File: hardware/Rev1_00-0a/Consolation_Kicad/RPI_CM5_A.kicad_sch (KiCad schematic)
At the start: 63 parts, among them J17 61300311121, J19 RPI_CMx_A, J7 2998TR, Q19 SSM3K56FS,LF, Q20 SSM3K56FS,LF, Q21 SSM3K56FS,LF, Q22 SSM3K56FS,LF, Q26 SSM3K56FS,LF, Q27 SSM3K56FS,LF, Q28 SSM3K56FS,LF, Q29 SSM3K56FS,LF, U19 SN74LVC1G125DBVR, U21 MCP7940NT-I/MS, Y2 32.768kHz

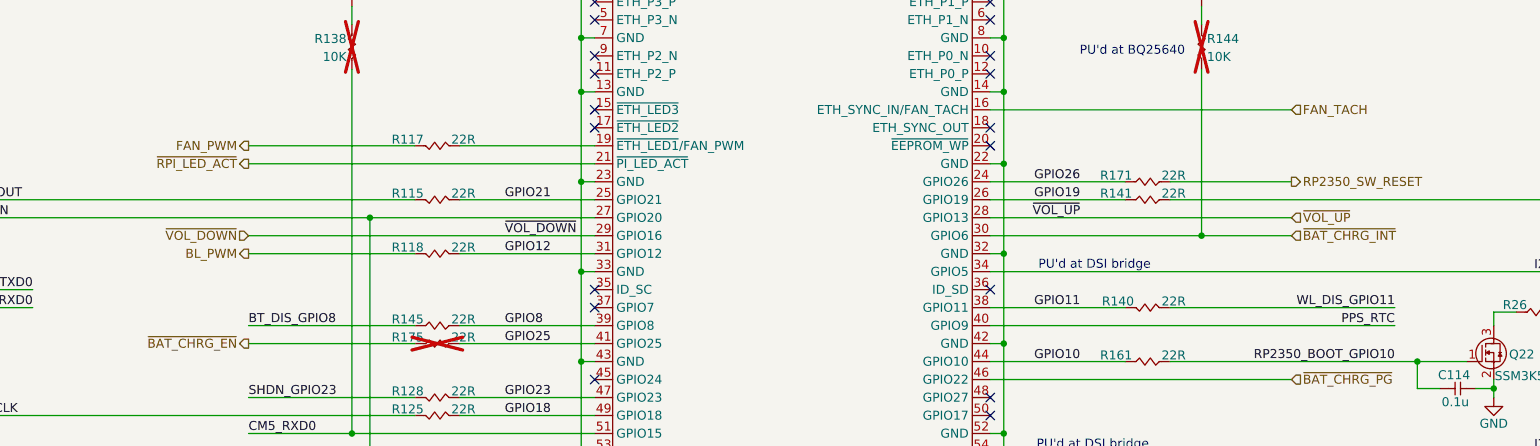
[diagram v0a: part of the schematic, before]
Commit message: Routing Adjust PinMux to ease routing
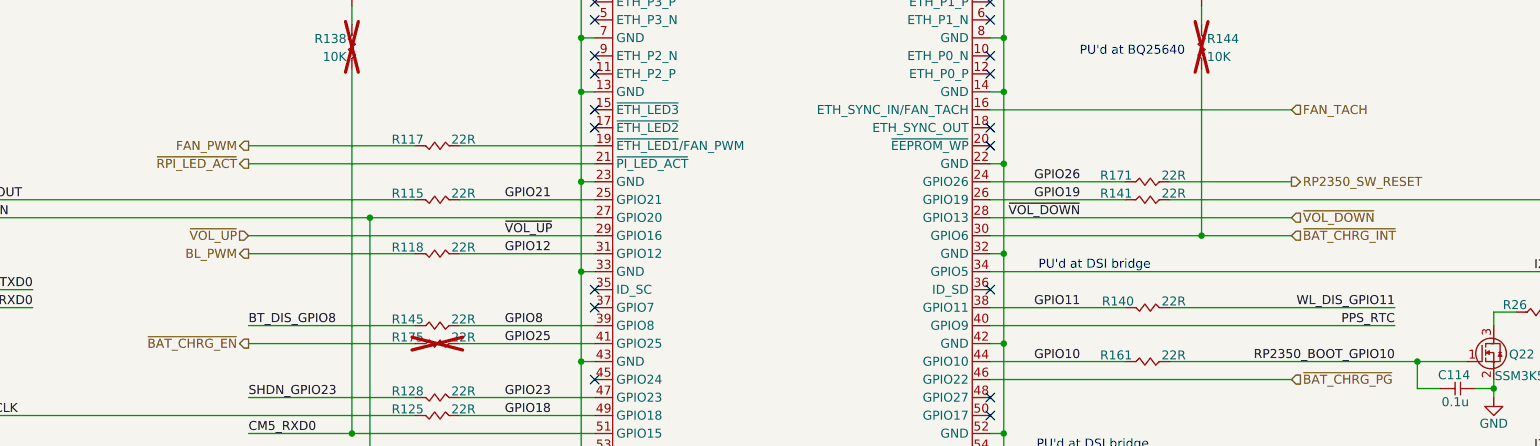
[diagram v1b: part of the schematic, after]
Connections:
- net ~{VOL_DOWN}: now also J19.28 (GPIO13); no longer J19.29 (GPIO16)
- net ~{VOL_UP}: now also J19.29 (GPIO16); no longer J19.28 (GPIO13)
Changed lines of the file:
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@@
 	(title_block
 		(title "Consolation [Console Emulation]")
-		(date "2026-10-12")
+		(date "2026-10-25")
 		(rev "1.00-0A")
 		(comment 1 "Jean-Francois Bilodeau")
@@
 	)
 	(bus_entry
+		(at 31.115 75.565)
+		(size 2.54 2.54)
+		(stroke
+			(width 0)
+			(type default)
+		)
+	)
+	(bus_entry
 		(at 31.115 85.725)
 		(size 2.54 2.54)
@@
 	)
 	(bus_entry
-		(at 31.115 75.565)
-		(size 2.54 2.54)
-		(stroke
-			(width 0)
-			(type default)
-		)
-	)
-	(bus_entry
 		(at 31.115 90.805)
 		(size 2.54 2.54)
@@
 		)
 	)
-	(bus
-		(pts
-			(xy 28.575 73.025) (xy 31.115 75.565)
-		)
-		(stroke
-			(width 0)
-			(type default)
-		)
-	)
 	(wire
 		(pts
@@
 	(wire
 		(pts
-			(xy 33.655 78.105) (xy 97.79 78.105)
+			(xy 106.045 172.085) (xy 107.315 172.085)
 		)
 		(stroke
@@
 	(wire
 		(pts
-			(xy 106.045 172.085) (xy 107.315 172.085)
+			(xy 137.795 178.435) (xy 137.795 184.15)
 		)
 		(stroke
@@
 	(wire
 		(pts
-			(xy 137.795 178.435) (xy 137.795 184.15)
+			(xy 29.21 139.065) (xy 29.21 142.875)
 		)
 		(stroke
@@
 	(wire
 		(pts
-			(xy 29.21 139.065) (xy 29.21 142.875)
+			(xy 33.655 50.165) (xy 91.44 50.165)
 		)
 		(stroke
@@
 	(wire
 		(pts
-			(xy 33.655 50.165) (xy 91.44 50.165)
+			(xy 102.235 118.745) (xy 102.235 120.015)
 		)
 		(stroke
@@
 	(wire
 		(pts
-			(xy 102.235 118.745) (xy 102.235 120.015)
+			(xy 239.395 159.385) (xy 239.395 160.655)
 		)
 		(stroke
@@
 	(wire
 		(pts
-			(xy 239.395 159.385) (xy 239.395 160.655)
+			(xy 179.07 83.185) (xy 268.605 83.185)
 		)
 		(stroke
@@
 	(wire
 		(pts
-			(xy 179.07 83.185) (xy 268.605 83.185)
+			(xy 33.655 78.105) (xy 97.79 78.105)
 		)
 		(stroke
@@
 		)
 	)
+	(bus
+		(pts
+			(xy 28.575 73.025) (xy 31.115 75.565)
+		)
+		(stroke
+			(width 0)
+			(type default)
+		)
+	)
 	(wire
 		(pts
@@
 		)
 	)
-	(label "~{VOL_DOWN}"
+	(label "~{VOL_UP}"
 		(at 110.49 52.705 0)
 		(effects
@@
 		)
 	)
-	(label "~{VOL_UP}"
+	(label "~{VOL_DOWN}"
 		(at 191.77 50.165 180)
 		(effects
@@
 		)
 	)
-	(hierarchical_label "~{VOL_DOWN}"
+	(hierarchical_label "~{VOL_UP}"
 		(shape input)
 		(at 74.295 52.705 180)
@@
 		)
 	)
-	(hierarchical_label "~{VOL_UP}"
+	(hierarchical_label "~{VOL_DOWN}"
 		(shape input)
 		(at 221.615 50.165 0)

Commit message: Add preliminary manufacturing files for Consolation Review pinout & design notes
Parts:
- added R165: 10K, footprint:RES_0402, symbol KicadCompDb:Resistors/RES_SMT_00013
- R144: now fitted
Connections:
- net 3V3: now also R165.2
- net ~{BAT_CHRG_PG}: now also R165.1
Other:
- note removed: "PU'd at BQ25640"

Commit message: Work on DFM, Pick N Place file accuracy, BOM accuracy Generating output files regularly through incremental updates
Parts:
- J19: value RPI_CMx_A -> DF40HC(3.0)-100DS-0.4V
- TP54, TP55: now left out of the parts list
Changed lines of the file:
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@@
 		(body_style 1)
 		(exclude_from_sim no)
-		(in_bom yes)
+		(in_bom no)
 		(on_board yes)
-		(in_pos_files yes)
+		(in_pos_files no)
 		(dnp no)
 		(property "Reference" "TP54"
@@
 			)
 		)
-		(property "Value" "RPI_CMx_A"
-			(at 171.323 14.859 0)
+		(property "Value" "DF40HC(3.0)-100DS-0.4V"
+			(at 163.83 14.986 0)
 			(show_name no)
 			(do_not_autoplace no)
@@
 		(body_style 1)
 		(exclude_from_sim no)
-		(in_bom yes)
+		(in_bom no)
 		(on_board yes)
-		(in_pos_files yes)
+		(in_pos_files no)
 		(dnp no)
 		(property "Reference" "TP55"
